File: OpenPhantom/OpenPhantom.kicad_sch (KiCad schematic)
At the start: 107 parts, among them J1 Barrel_Jack, J2 Video, J3 Audio, Q1 BC548, Q2 BD136, Q3 BC557, Q4 BC548, SW1 POWER, SW2 RESET, U1 UM6116 VRAM, U10 74HC368, U11 74HC368, U2 UM6116 WRAM, U3 74HC04, U4 UA6547_CPU, U5 4013, U6 UA6548_PPU, U7 74HC139, U8 74LS373, U9 LM7805_TO220, Y1 21.453366 MHz

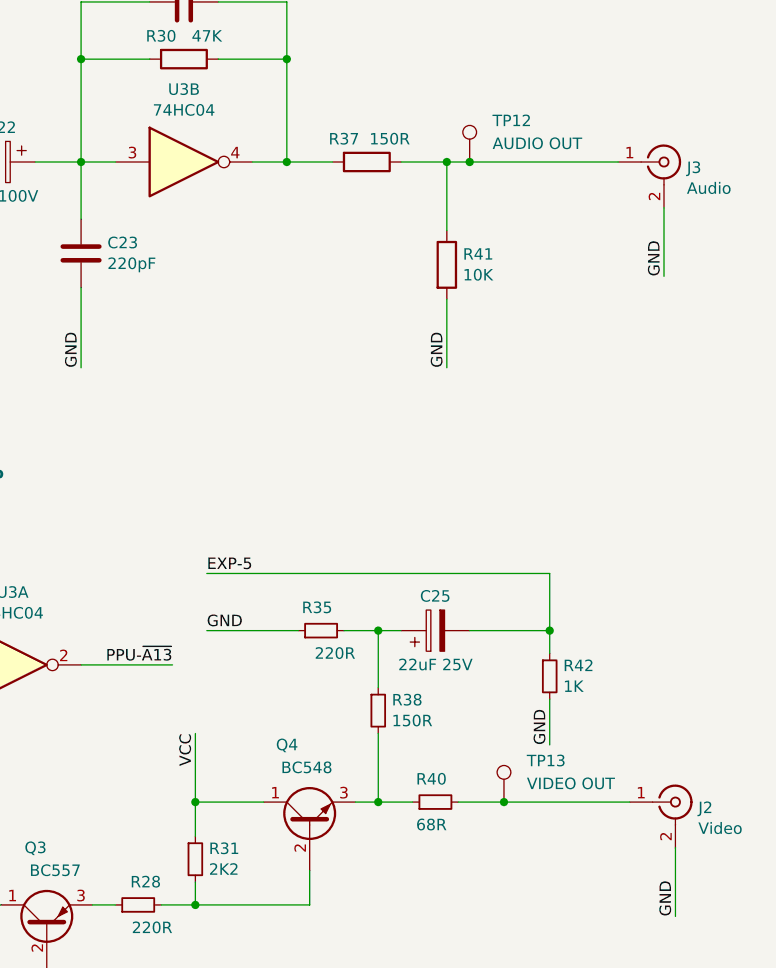
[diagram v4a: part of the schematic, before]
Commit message: Added C26 + RF circuit removed
Added C26 removed RF circuit components fixing audio noise.
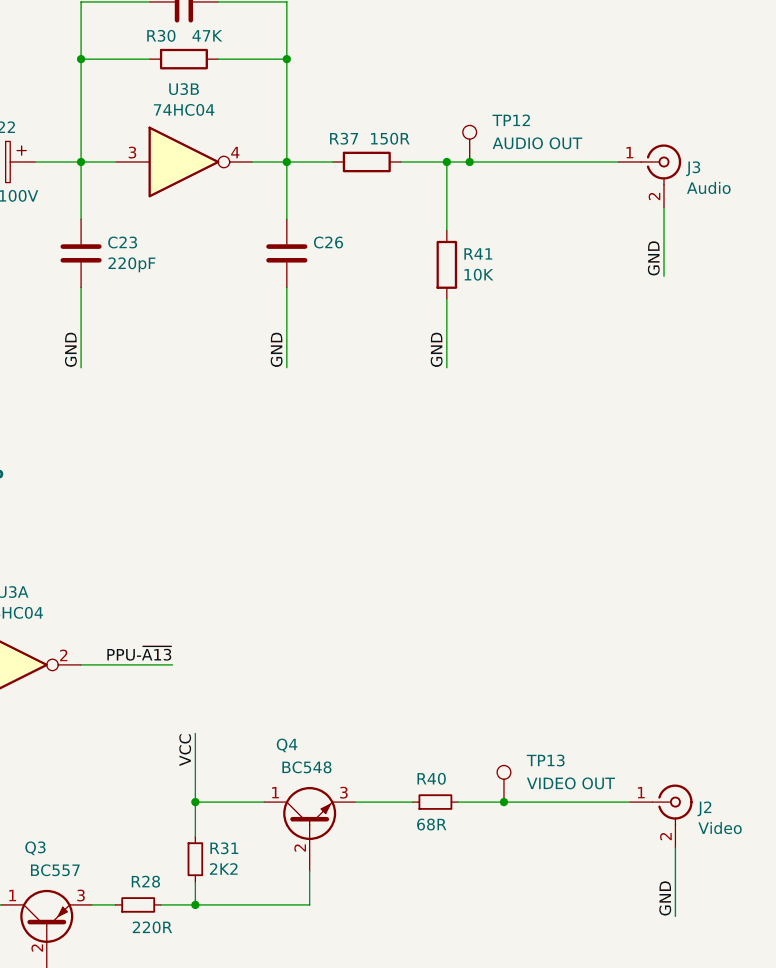
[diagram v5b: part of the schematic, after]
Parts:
- removed C25: 22uF 25V, Capacitor_THT:CP_Radial_D5.0mm_P2.50mm, symbol Device:CP
- removed R35: 220R, Resistor_THT:R_Axial_DIN0207_L6.3mm_D2.5mm_P10.16mm_Horizontal, symbol Device:R_Small
- removed R38: 150R, Resistor_THT:R_Axial_DIN0207_L6.3mm_D2.5mm_P10.16mm_Horizontal, symbol Device:R_Small
- removed R42: 1K, Resistor_THT:R_Axial_DIN0207_L6.3mm_D2.5mm_P10.16mm_Horizontal, symbol Device:R_Small
- added C26: (no value), Capacitor_THT:C_Disc_D4.7mm_W2.5mm_P5.00mm, symbol Device:C
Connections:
- net GND: now also C26.2
- net at C24.1, R30.1, R37.2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: now also C26.1

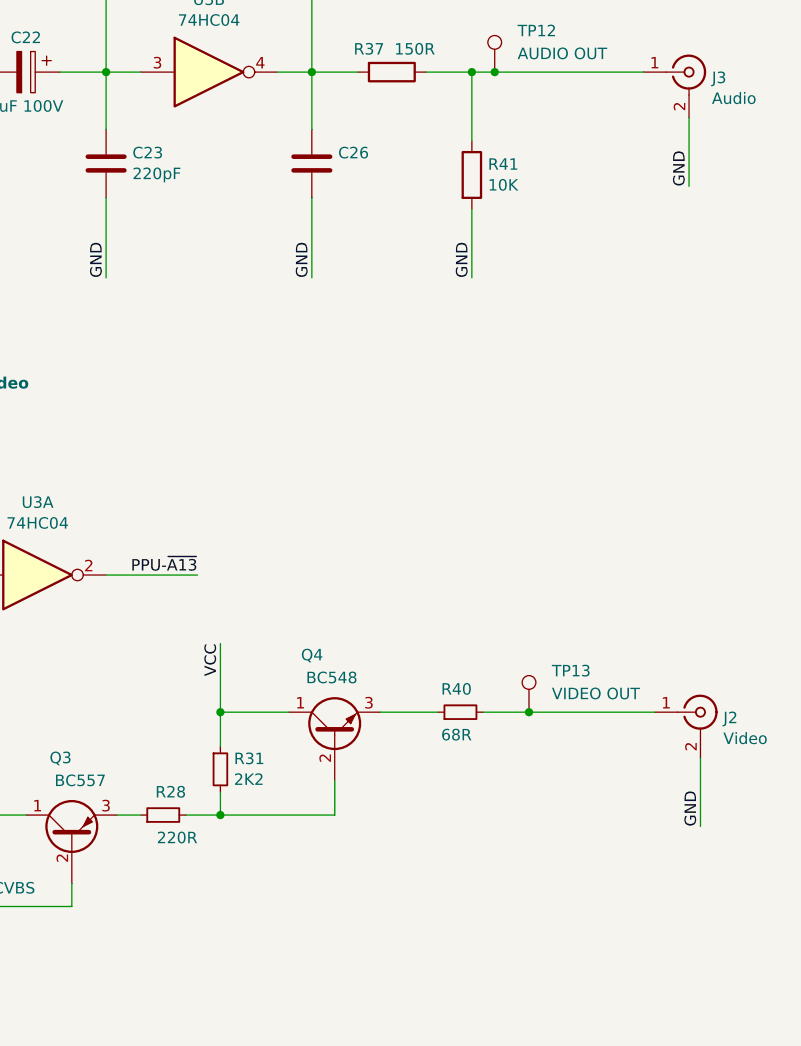
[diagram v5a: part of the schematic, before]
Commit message: Added R35
Added R35 to improved image quality.
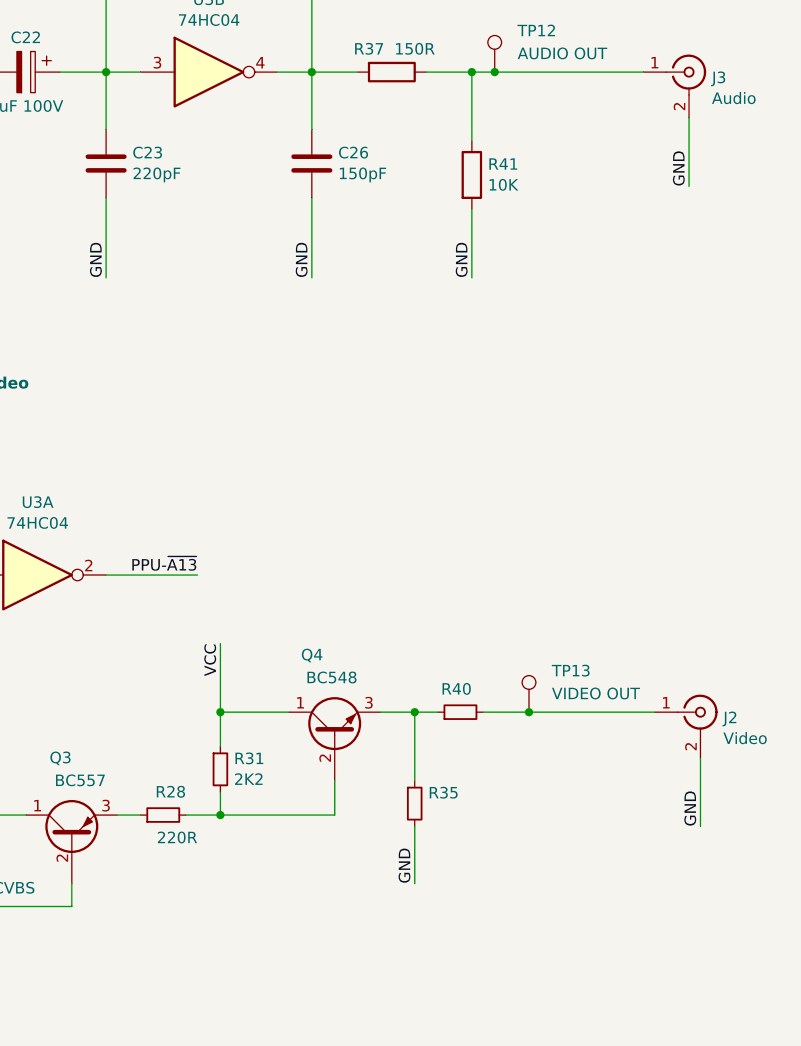
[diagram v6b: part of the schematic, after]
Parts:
- added R35: (no value), Resistor_THT:R_Axial_DIN0207_L6.3mm_D2.5mm_P10.16mm_Horizontal, symbol Device:R_Small
- C26: value (none) -> 150pF
- R40: value 68R -> (none)
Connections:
- net GND: now also R35.2
- net at Q4.3 (E), R40.1: now also R35.1
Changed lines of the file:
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@@
   (title_block
     (title "OpenPhantom - Gradiente Phantom System PH-8 Main Board")
-    (date "2022-06-22")
-    (rev "5")
+    (date "2022-11-12")
+    (rev "7")
     (comment 1 "Twitter: @vagnerlc")
     (comment 2 "github.com/vlcampos/OpenPhantom")
     (comment 3 "Project files at/Arquivos do projeto em:")
+    (comment 4 "Rev. 7 - Added R35")
   )
   (junction (at 351.79 85.09) (diameter 0) (color 0 0 0 0)
@@
   (junction (at 341.63 77.47) (diameter 0) (color 0 0 0 0)
   )
+  (junction (at 367.03 201.93) (diameter 0) (color 0 0 0 0)
+  )
   (junction (at 313.69 223.52) (diameter 0) (color 0 0 0 0)
   )
@@
     (stroke (width 0) (type default) (color 0 0 0 0))
   )
+  (wire (pts (xy 367.03 201.93) (xy 369.57 201.93))
+    (stroke (width 0) (type default) (color 0 0 0 0))
+  )
   (wire (pts (xy 138.43 58.42) (xy 128.27 58.42))
     (stroke (width 0) (type default) (color 0 0 0 0))
@@
     (stroke (width 0) (type default) (color 0 0 0 0))
   )
+  (wire (pts (xy 367.03 201.93) (xy 367.03 209.55))
+    (stroke (width 0) (type default) (color 0 0 0 0))
+  )
   (wire (pts (xy 210.82 38.1) (xy 223.52 38.1))
     (stroke (width 0) (type default) (color 0 0 0 0))
@@
     (stroke (width 0) (type default) (color 0 0 0 0))
   )
-  (wire (pts (xy 363.22 201.93) (xy 369.57 201.93))
+  (wire (pts (xy 363.22 201.93) (xy 367.03 201.93))
     (stroke (width 0) (type default) (color 0 0 0 0))
   )
@@
     (stroke (width 0) (type default) (color 0 0 0 0))
   )
+  (wire (pts (xy 367.03 214.63) (xy 367.03 220.98))
+    (stroke (width 0) (type default) (color 0 0 0 0))
+  )
   (wire (pts (xy 60.96 111.76) (xy 76.2 111.76))
     (stroke (width 0) (type default) (color 0 0 0 0))
@@
     (effects (font (size 1.27 1.27)) (justify left bottom))
   )
+  (label "GND" (at 367.03 220.98 90)
+    (effects (font (size 1.27 1.27)) (justify left bottom))
+  )
   (label "CPU-A12" (at 76.2 106.68 180)
     (effects (font (size 1.27 1.27)) (justify right bottom))
@@
       (effects (font (size 1.27 1.27)) (justify left))
     )
-    (property "Value" "68R" (id 1) (at 373.38 204.47 90)
+    (property "Value" "" (id 1) (at 373.38 204.47 90)
       (effects (font (size 1.27 1.27)) (justify left))
     )
@@
       (effects (font (size 1.27 1.27)) (justify left))
     )
-    (property "Value" "" (id 1) (at 358.521 142.113 0)
+    (property "Value" "150pF" (id 1) (at 358.521 142.113 0)
       (effects (font (size 1.27 1.27)) (justify left))
     )
@@
     (pin "1")
   )
+  (symbol (lib_id "Device:R_Small") (at 367.03 212.09 0) (unit 1)
+    (in_bom yes) (on_board yes)
+    (property "Reference" "R35" (id 0) (at 368.5286 210.9216 0)
+      (effects (font (size 1.27 1.27)) (justify left))
+    )
+    (property "Value" "" (id 1) (at 368.5286 213.233 0)
+      (effects (font (size 1.27 1.27)) (justify left))
+    )
+    (property "Footprint" "Resistor_THT:R_Axial_DIN0207_L6.3mm_D2.5mm_P10.16mm_Horizontal" (id 2) (at 367.03 212.09 0)
+      (effects (font (size 1.27 1.27)) hide)
+    )
+    (property "Datasheet" "~" (id 3) (at 367.03 212.09 0)
+      (effects (font (size 1.27 1.27)) hide)
+    )
+    (pin "1")
+    (pin "2")
+  )
   (symbol (lib_id "Connector:TestPoint") (at 276.86 134.62 0) (unit 1)
     (in_bom yes) (on_board yes) (fields_autoplaced)
@@
       (reference "R34") (unit 1) (value "10K") (footprint "Resistor_THT:R_Axial_DIN0207_L6.3mm_D2.5mm_P10.16mm_Horizontal")
     )
+    (path "/e53bcdb9-0b81-4541-afca-58f9ea0cc3e5"
+      (reference "R35") (unit 1) (value "150R") (footprint "Resistor_THT:R_Axial_DIN0207_L6.3mm_D2.5mm_P10.16mm_Horizontal")
+    )
     (path "/00000000-0000-0000-0000-000063672877"

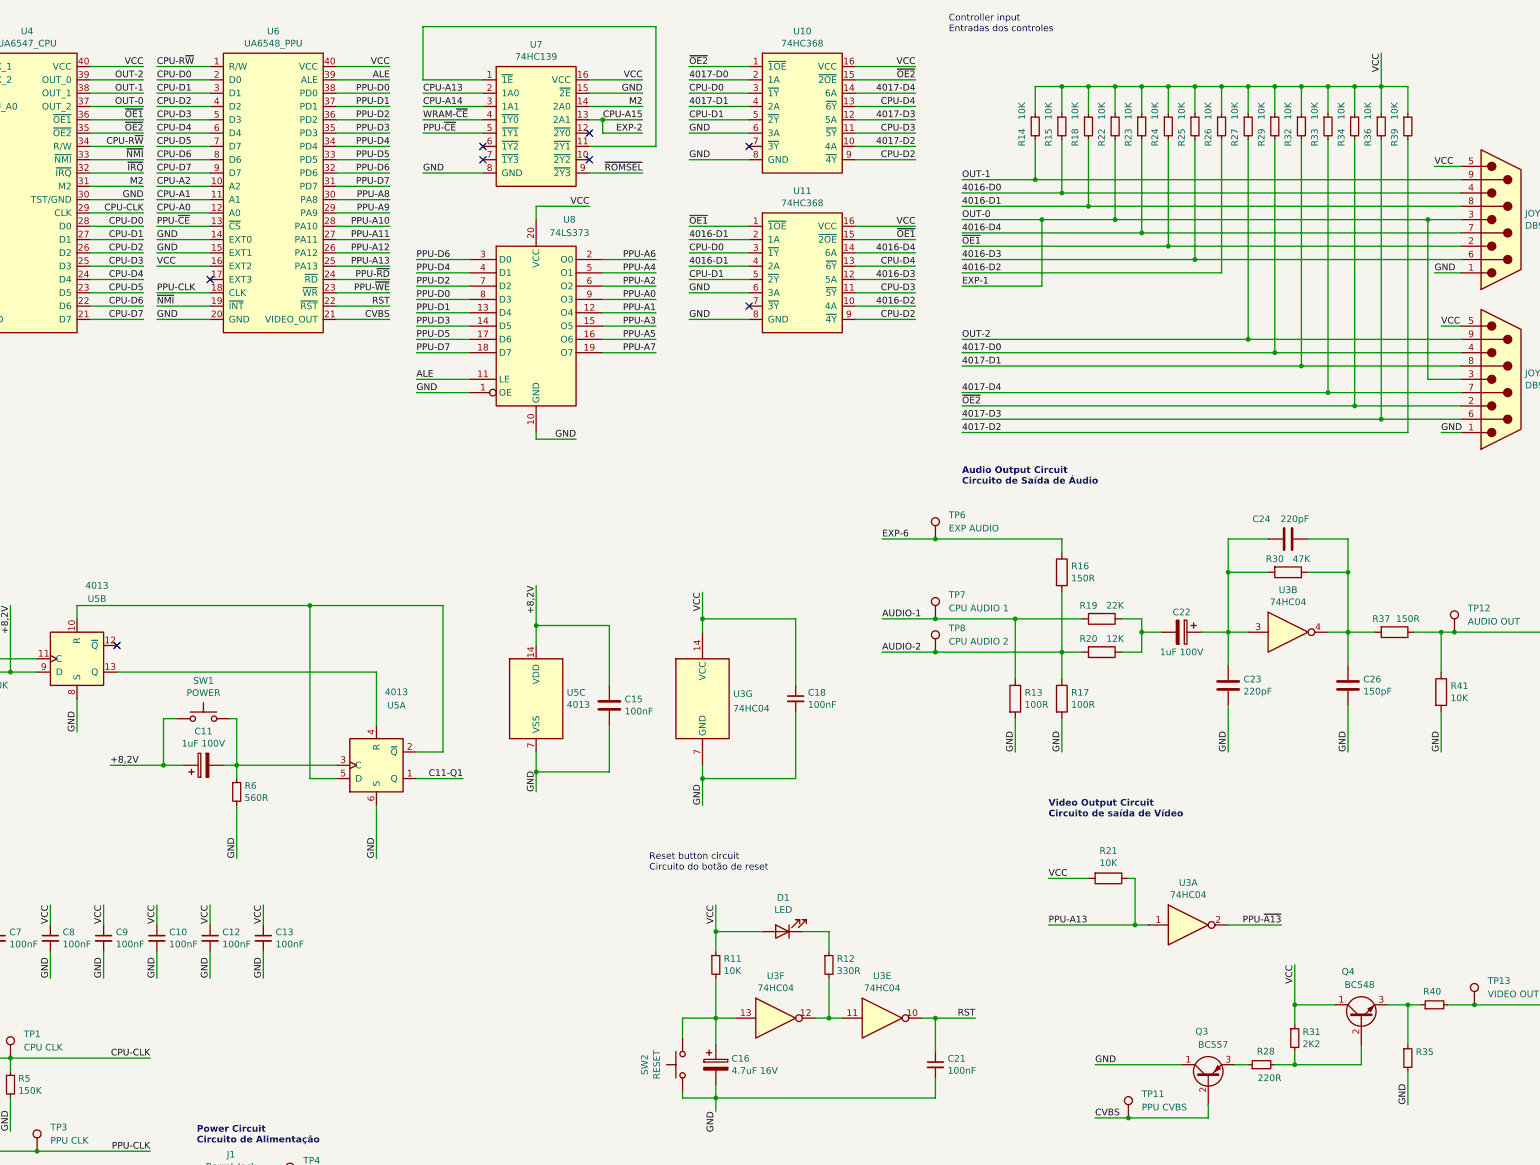
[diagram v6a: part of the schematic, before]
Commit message: Player controller fixed
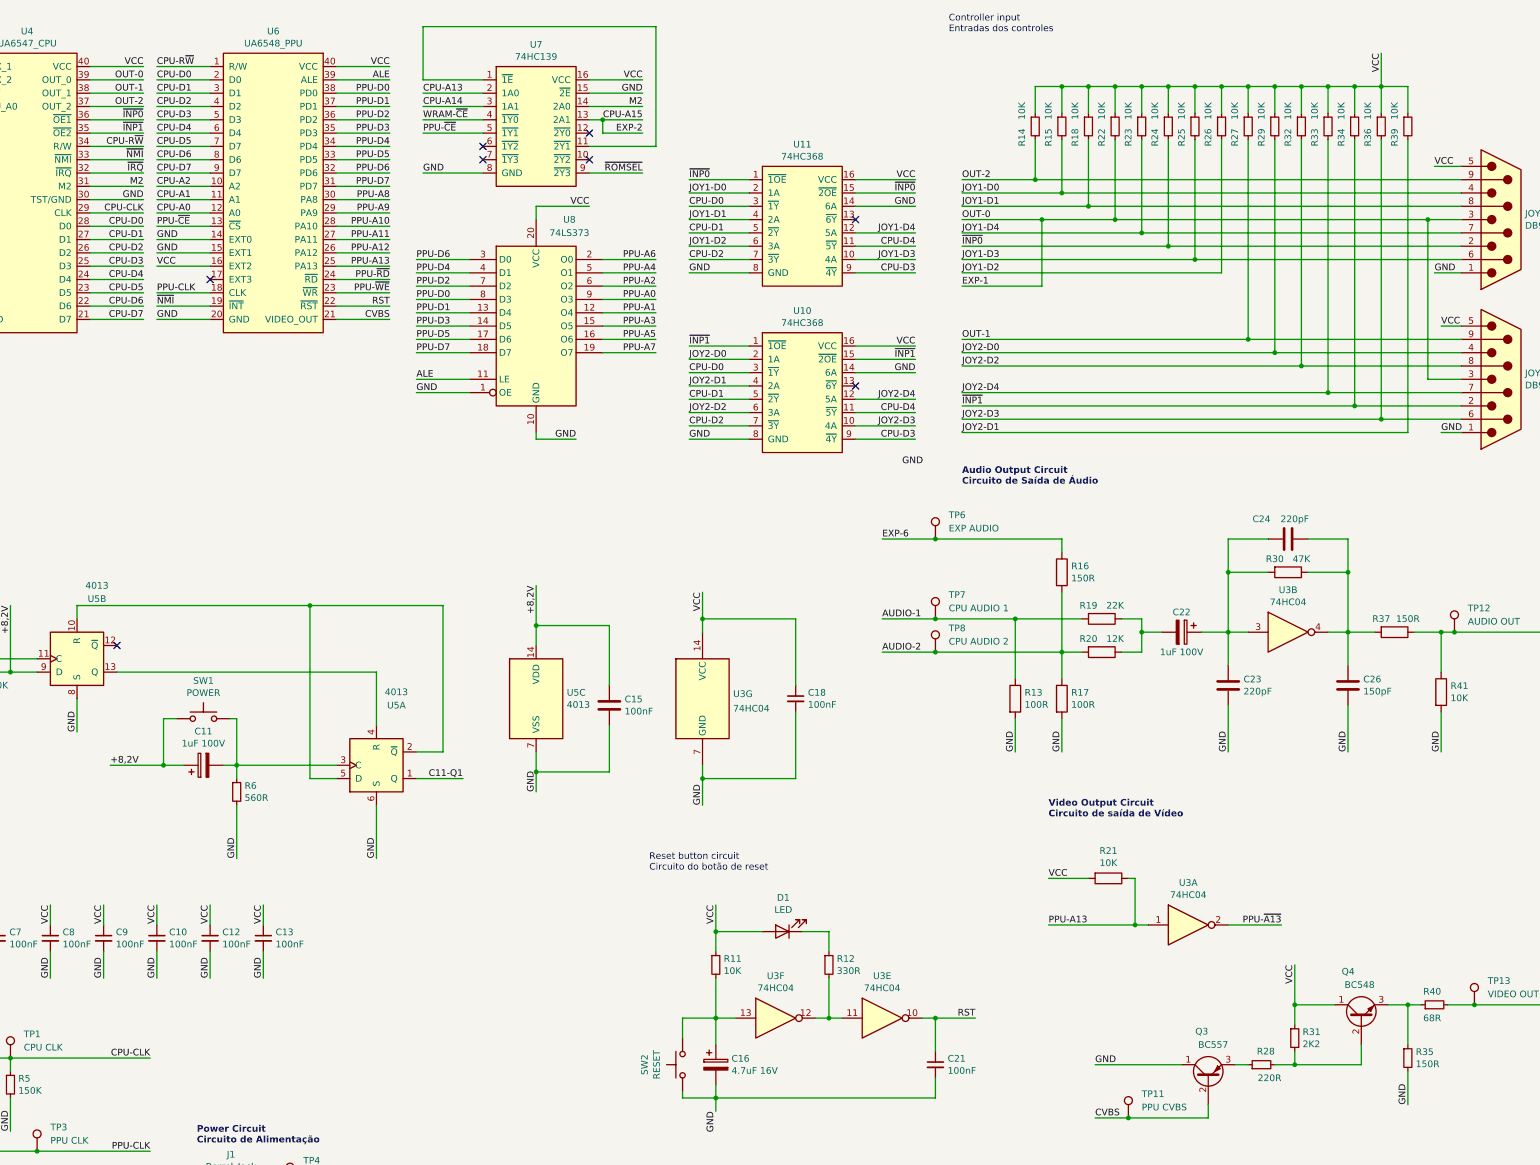
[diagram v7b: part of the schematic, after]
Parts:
- R35: value (none) -> 150R
- R40: value (none) -> 68R
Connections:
- net CPU-D2: now also U10.7 (~{3Y}), U11.7 (~{3Y}); no longer U10.9 (~{4Y}), U11.9 (~{4Y})
- net CPU-D3: now also U10.9 (~{4Y}), U11.9 (~{4Y}); no longer U10.11 (~{5Y}), U11.11 (~{5Y})
- net CPU-D4: now also U10.11 (~{5Y}), U11.11 (~{5Y}); no longer U10.13 (~{6Y}), U11.13 (~{6Y})
- net EXP-1: now also U4.39 (OUT_0); no longer U4.37 (OUT_2)
- net GND: now also U10.14 (6A), U11.14 (6A); no longer U10.6 (3A), U11.6 (3A)
- net OUT-1: now also JOY2.9, R27.2; no longer JOY1.9, R14.2
- net OUT-2: now also JOY1.9, R14.2, U4.37 (OUT_2); no longer JOY2.9, R27.2, U4.39 (OUT_0)
- net 4016-D0 renamed JOY1-D0
- net JOY1-D0: now also U11.2 (1A)
- net 4016-D1 renamed JOY1-D1
- net JOY1-D1: no longer U11.2 (1A)
- net 4016-D2 renamed JOY1-D2
- net JOY1-D2: now also U11.6 (3A); no longer U11.10 (4A)
- net 4016-D3 renamed JOY1-D3
- net JOY1-D3: now also U11.10 (4A); no longer U11.12 (5A)
- net 4016-D4 renamed JOY1-D4
- net JOY1-D4: now also U11.12 (5A); no longer U11.14 (6A)
- net 4017-D0 renamed JOY2-D0
- net 4017-D1 renamed JOY2-D2
- net JOY2-D2: now also U10.6 (3A); no longer U10.4 (2A)
- net 4017-D2 renamed JOY2-D1
- net JOY2-D1: now also U10.4 (2A); no longer U10.10 (4A)
- net 4017-D3 renamed JOY2-D3
- net JOY2-D3: now also U10.10 (4A); no longer U10.12 (5A)
- net 4017-D4 renamed JOY2-D4
- net JOY2-D4: now also U10.12 (5A); no longer U10.14 (6A)
- net ~{OE1} renamed ~{INP0}
- net ~{OE2} renamed ~{INP1}
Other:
- moved on the sheet: U10, U11
